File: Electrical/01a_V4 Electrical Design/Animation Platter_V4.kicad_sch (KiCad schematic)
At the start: 0 parts

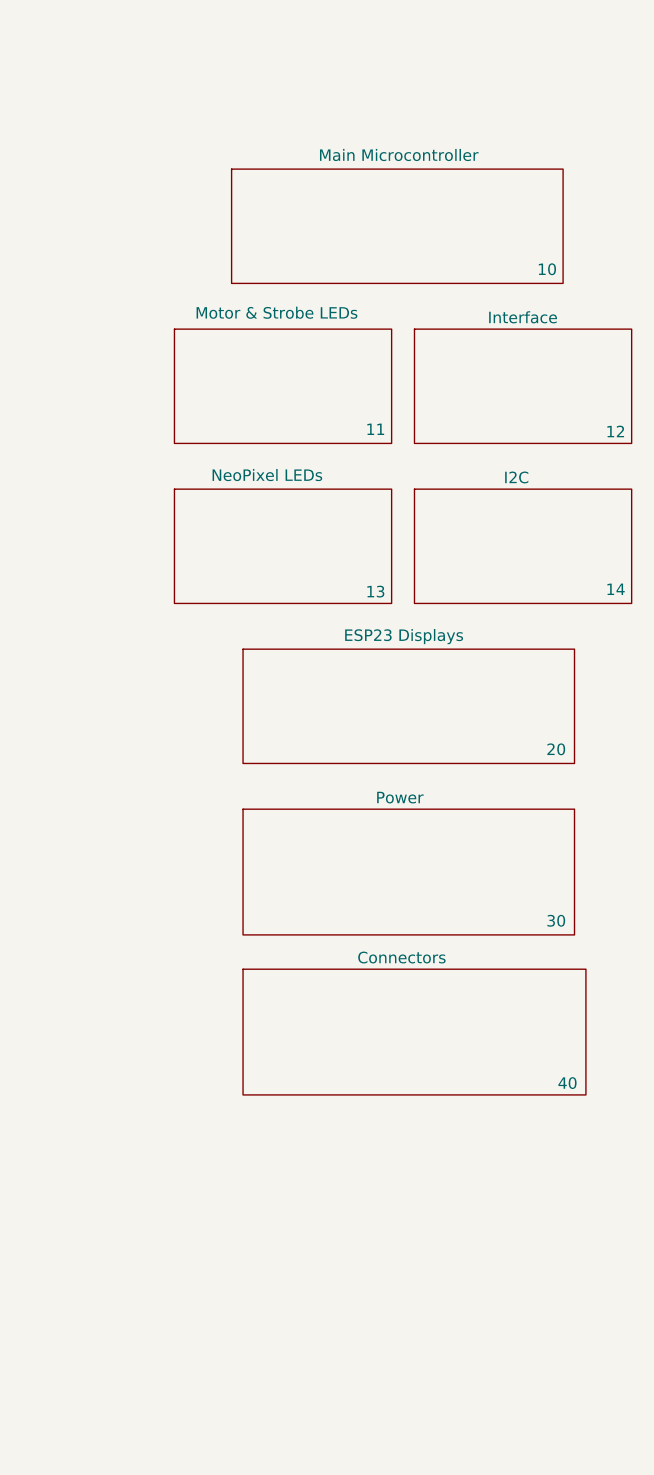
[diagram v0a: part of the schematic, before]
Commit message: updates to schematic to document outside components. Plans for additional electrical features requiring desiging a few more PCBs
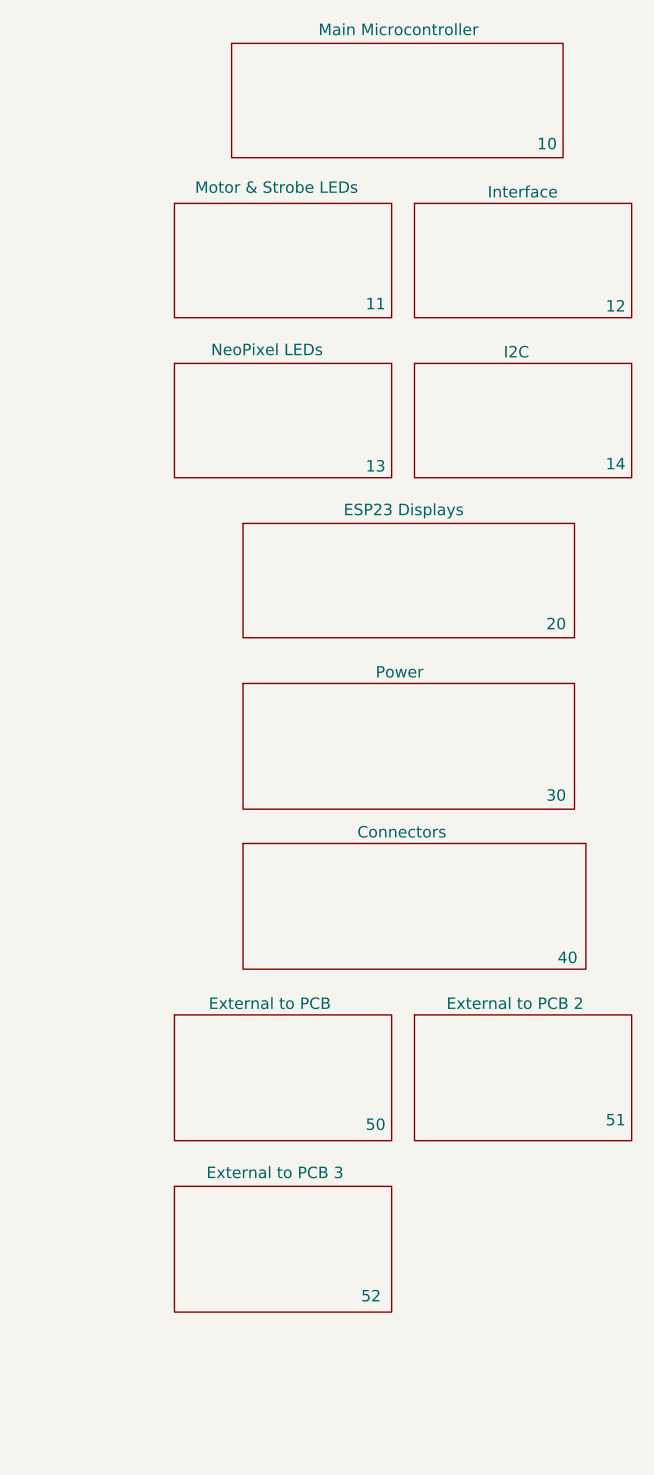
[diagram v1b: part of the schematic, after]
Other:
- added sheet External to PCB (External to PCB.kicad_sch)
- added sheet External to PCB 2 (External to PCB 2.kicad_sch)
- added sheet External to PCB 3 (External to PCB 3.kicad_sch)
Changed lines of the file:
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@@
 	)
 	(sheet
-		(at 207.01 68.58)
+		(at 207.01 54.61)
 		(size 24.13 12.7)
 		(exclude_from_sim no)
@@
 		)
 		(property "Sheetname" "NeoPixel LEDs"
-			(at 211.074 67.818 0)
+			(at 211.074 53.848 0)
 			(effects
 				(font
@@
 		)
 		(property "Sheetfile" "Display and LEDs.kicad_sch"
-			(at 207.01 81.8646 0)
+			(at 207.01 67.8946 0)
 			(effects
 				(font
@@
 		)
 		(property "Field2" "13"
-			(at 229.362 80.01 0)
+			(at 229.362 66.04 0)
 			(effects
 				(font
@@
 	)
 	(sheet
-		(at 233.68 68.58)
+		(at 207.01 127)
+		(size 24.13 13.97)
+		(exclude_from_sim no)
+		(in_bom no)
+		(on_board no)
+		(dnp no)
+		(stroke
+			(width 0.1524)
+			(type solid)
+		)
+		(fill
+			(color 0 0 0 0.0000)
+		)
+		(property "Sheetname" "External to PCB"
+			(at 210.82 126.492 0)
+			(effects
+				(font
+					(size 1.27 1.27)
+				)
+				(justify left bottom)
+			)
+		)
+		(property "Sheetfile" "External to PCB.kicad_sch"
+			(at 207.01 140.7926 0)
+			(effects
+				(font
+					(size 1.27 1.27)
+				)
+				(justify left top)
+				(hide yes)
+			)
+		)
+		(property "Field2" "50"
+			(at 229.362 139.192 0)
+			(effects
+				(font
+					(size 1.27 1.27)
+				)
+			)
+		)
+		(instances
+			(project "Animation Platter_V4"
+				(path "/6293f612-ad61-4760-ad66-c804a0624dd1"
+					(page "50")
+				)
+			)
+		)
+	)
+	(sheet
+		(at 233.68 54.61)
 		(size 24.13 12.7)
 		(exclude_from_sim no)
@@
 		)
 		(property "Sheetname" "I2C"
-			(at 243.586 68.072 0)
+			(at 243.586 54.102 0)
 			(effects
 				(font
@@
 		)
 		(property "Sheetfile" "I2C RTC.kicad_sch"
-			(at 233.68 83.1346 0)
+			(at 233.68 69.1646 0)
 			(effects
 				(font
@@
 		)
 		(property "Field2" "14"
-			(at 256.032 79.756 0)
+			(at 256.032 65.786 0)
 			(effects
 				(font
@@
 	)
 	(sheet
-		(at 214.63 86.36)
+		(at 214.63 72.39)
 		(size 36.83 12.7)
 		(exclude_from_sim no)
@@
 		)
 		(property "Sheetname" "ESP23 Displays"
-			(at 225.806 85.598 0)
+			(at 225.806 71.628 0)
 			(effects
 				(font
@@
 		)
 		(property "Sheetfile" "ESP32 Displays.kicad_sch"
-			(at 214.63 99.6446 0)
+			(at 214.63 85.6746 0)
 			(effects
 				(font
@@
 		)
 		(property "Field2" "20"
-			(at 249.428 97.536 0)
+			(at 249.428 83.566 0)
 			(effects
 				(font
@@
 	)
 	(sheet
-		(at 213.36 33.02)
+		(at 213.36 19.05)
 		(size 36.83 12.7)
 		(exclude_from_sim no)
@@
 		)
 		(property "Sheetname" "Main Microcontroller"
-			(at 231.902 32.258 0)
+			(at 231.902 18.288 0)
 			(effects
 				(font
@@
 		)
 		(property "Sheetfile" "Microcontroller.kicad_sch"
-			(at 213.36 46.3046 0)
+			(at 213.36 32.3346 0)
 			(effects
 				(font
@@
 		)
 		(property "sheetNumber" "10"
-			(at 248.412 44.196 0)
+			(at 248.412 30.226 0)
 			(effects
 				(font
@@
 	)
 	(sheet
-		(at 214.63 104.14)
+		(at 207.01 146.05)
+		(size 24.13 13.97)
+		(exclude_from_sim no)
+		(in_bom no)
+		(on_board no)
+		(dnp no)
+		(stroke
+			(width 0.1524)
+			(type solid)
+		)
+		(fill
+			(color 0 0 0 0.0000)
+		)
+		(property "Sheetname" "External to PCB 3"
+			(at 210.566 145.288 0)
+			(effects
+				(font
+					(size 1.27 1.27)
+				)
+				(justify left bottom)
+			)
+		)
+		(property "Sheetfile" "External to PCB 3.kicad_sch"
+			(at 207.01 159.8426 0)
+			(effects
+				(font
+					(size 1.27 1.27)
+				)
+				(justify left top)
+				(hide yes)
+			)
+		)
+		(property "Field2" "52"
+			(at 228.854 158.242 0)
+			(effects
+				(font
+					(size 1.27 1.27)
+				)
+			)
+		)
+		(instances
+			(project "Animation Platter_V4"
+				(path "/6293f612-ad61-4760-ad66-c804a0624dd1"
+					(page "52")
+				)
+			)
+		)
+	)
+	(sheet
+		(at 214.63 90.17)
 		(size 36.83 13.97)
 		(exclude_from_sim no)
@@
 		)
 		(property "Sheetname" "Power"
-			(at 229.362 103.632 0)
+			(at 229.362 89.662 0)
 			(effects
 				(font
@@
 		)
 		(property "Sheetfile" "Power.kicad_sch"
-			(at 214.63 118.1866 0)
+			(at 214.63 104.2166 0)
 			(effects
 				(font
@@
 		)
 		(property "Field2" "30"
-			(at 249.428 116.586 0)
+			(at 249.428 102.616 0)
 			(effects
 				(font
@@
 	)
 	(sheet
-		(at 207.01 50.8)
+		(at 233.68 127)
+		(size 24.13 13.97)
+		(exclude_from_sim no)
+		(in_bom no)
+		(on_board no)
+		(dnp no)
+		(stroke
+			(width 0.1524)
+			(type solid)
+		)
+		(fill
+			(color 0 0 0 0.0000)
+		)
+		(property "Sheetname" "External to PCB 2"
+			(at 237.236 126.492 0)
+			(effects
+				(font
+					(size 1.27 1.27)
+				)
+				(justify left bottom)
+			)
+		)
+		(property "Sheetfile" "External to PCB 2.kicad_sch"
+			(at 233.68 140.7926 0)
+			(effects
+				(font
+					(size 1.27 1.27)
+				)
+				(justify left top)
+				(hide yes)
+			)
+		)
+		(property "Field2" "51"
+			(at 256.032 138.684 0)
+			(effects
+				(font
+					(size 1.27 1.27)
+				)
+			)
+		)
+		(instances
+			(project "Animation Platter_V4"
+				(path "/6293f612-ad61-4760-ad66-c804a0624dd1"
+					(page "51")
+				)
+			)
+		)
+	)
+	(sheet
+		(at 207.01 36.83)
 		(size 24.13 12.7)
 		(exclude_from_sim no)
@@
 		)
 		(property "Sheetname" "Motor & Strobe LEDs"
-			(at 209.296 49.784 0)
+			(at 209.296 35.814 0)
 			(effects
 				(font
@@
 		)
 		(property "Sheetfile" "Motor & LEDs_sch.kicad_sch"
-			(at 207.01 64.0846 0)
+			(at 207.01 50.1146 0)
 			(effects
 				(font
@@
 		)
 		(property "Field2" "11"
-			(at 229.362 61.976 0)
+			(at 229.362 48.006 0)
 			(effects
 				(font
@@
 	)
 	(sheet
-		(at 214.63 121.92)
+		(at 214.63 107.95)
 		(size 38.1 13.97)
 		(exclude_from_sim no)
@@
 		)
 		(property "Sheetname" "Connectors"
-			(at 227.33 121.412 0)
+			(at 227.33 107.442 0)
 			(effects
 				(font
@@
 		)
 		(property "Sheetfile" "Connectors.kicad_sch"
-			(at 214.63 135.7126 0)
+			(at 214.63 121.7426 0)
 			(effects
 				(font
@@
 		)
 		(property "Field2" "40"
-			(at 250.698 134.62 0)
+			(at 250.698 120.65 0)
 			(effects
 				(font
@@
 	)
 	(sheet
-		(at 233.68 50.8)
+		(at 233.68 36.83)
 		(size 24.13 12.7)
 		(exclude_from_sim no)
@@
 		)
 		(property "Sheetname" "Interface"
-			(at 241.808 50.292 0)
+			(at 241.808 36.322 0)
 			(effects
 				(font
@@
 		)
 		(property "Sheetfile" "Interface.kicad_sch"
-			(at 233.68 64.0846 0)
+			(at 233.68 50.1146 0)
 			(effects
 				(font
@@
 		)
 		(property "value" "12"
-			(at 256.032 62.23 0)
-			(effects
-				(font
+			(at 256.032 48.26 0)
+			(effects
+				(font

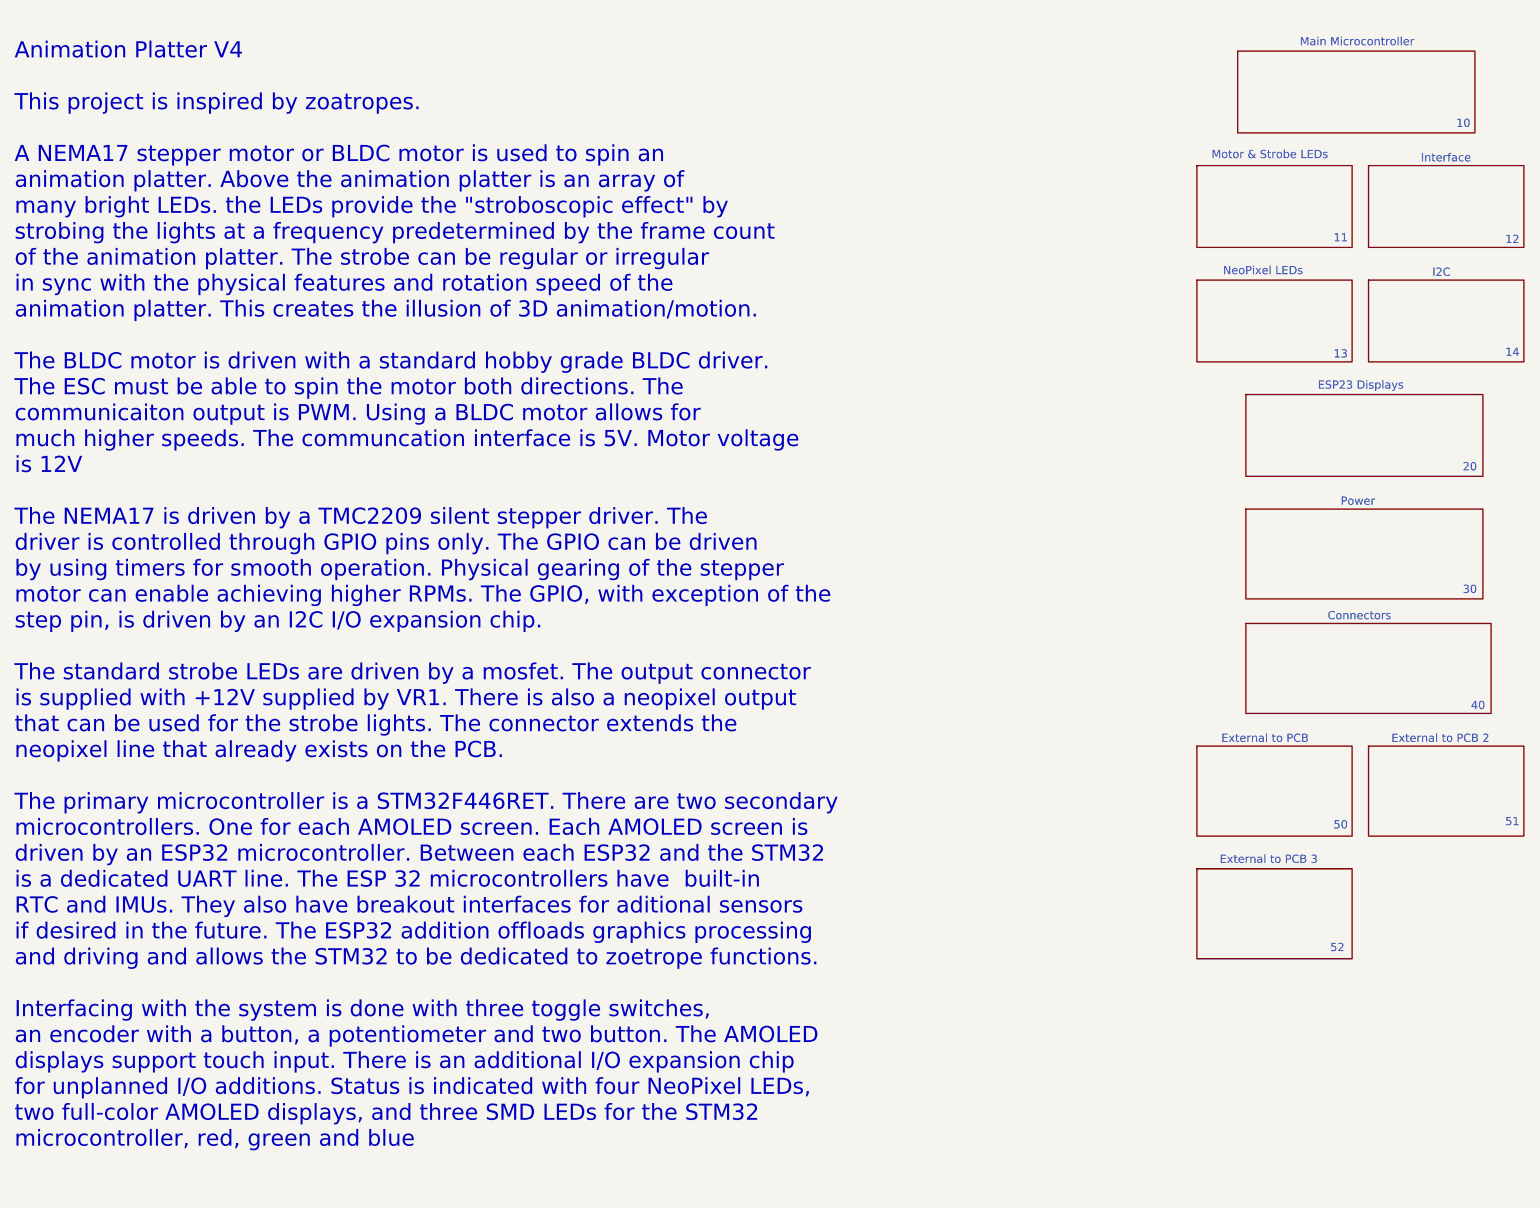
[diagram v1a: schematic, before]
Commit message: main schematic tweaks. Started the 'Saber' PCB which is the new end effector for the strobe light. Schematic nearly finished. Need to create footprint for LEDs and layout the board to be CNC milled.
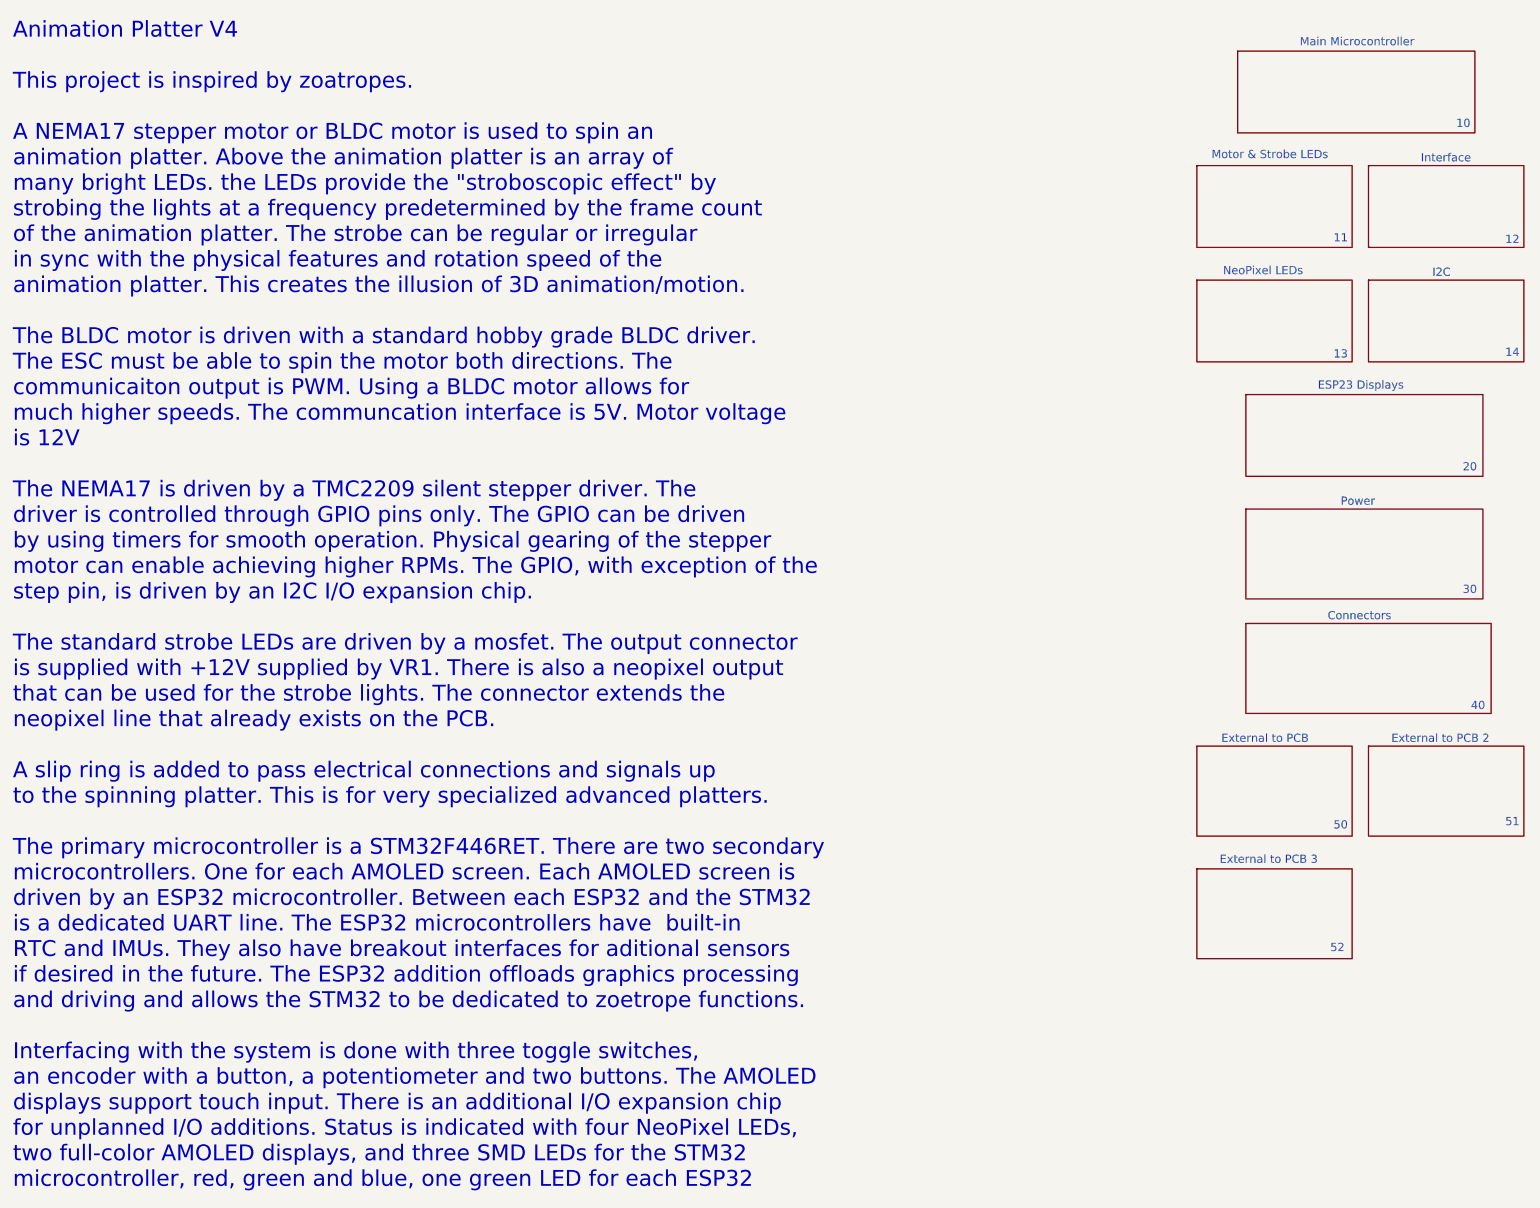
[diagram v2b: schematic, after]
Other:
- company: (none) -> Kadin Whiting
- title: (none) -> Zoetrope Carousel V4
